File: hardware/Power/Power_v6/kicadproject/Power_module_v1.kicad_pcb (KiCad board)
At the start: 2 copper layers, 70 x 39.2 mm, 63 parts, among them J1 Conn_01x02, J3 USB_B_Micro, J4 Conn_01x02_battery, J5 Conn_01x06_programmer, J6 Conn_01x06_programmer, J7 610106249121, U1 BQ24040, U2 BQ25570, U3 VEML7700-TT, U4 PIC16F18446

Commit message: Power module: HW update new pinheaders + new case
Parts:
- added REF**: MountingHole_3mm, MountingHole:MountingHole_3mm, F.Cu at (154.0, 78.0)
- J3: moved to F.Cu
- moved J3 10.9 mm to (105.7, 105.2), turned to 0 degrees
- moved C2 0.84 mm to (150.8, 78.0)
- moved C3 0.55 mm to (148.8, 78.0)
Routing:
- net VUSB: track 67.8 -> 72.8 mm, vias 4 -> 5
- net GND: track 207.3 -> 203.7 mm, vias 82 -> 89
- net 3V3: track 72.9 -> 75.0 mm
- net VEML7700_SDA: track 62.6 -> 64.4 mm
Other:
- board size 70 x 39.2 mm -> 67.2 x 39.2 mm

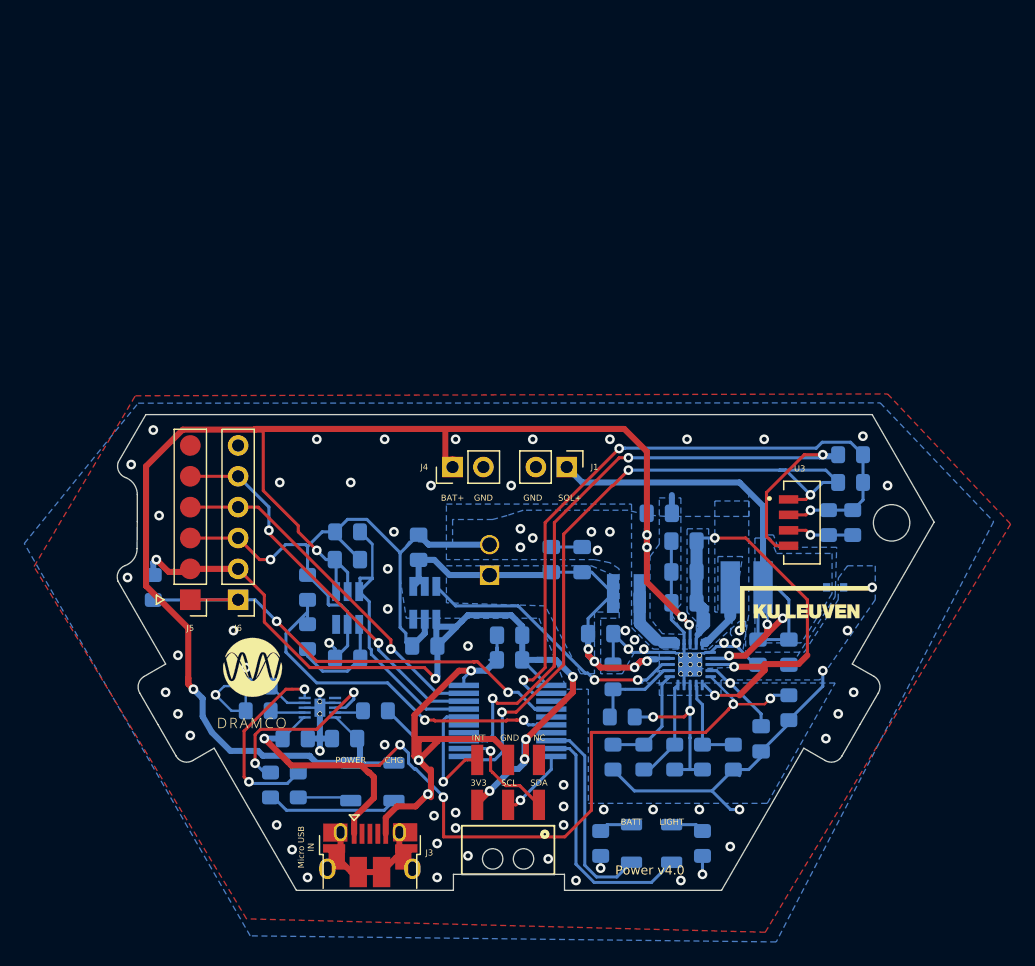
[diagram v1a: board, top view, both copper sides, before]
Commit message: Buttons + power HW update to support new casing
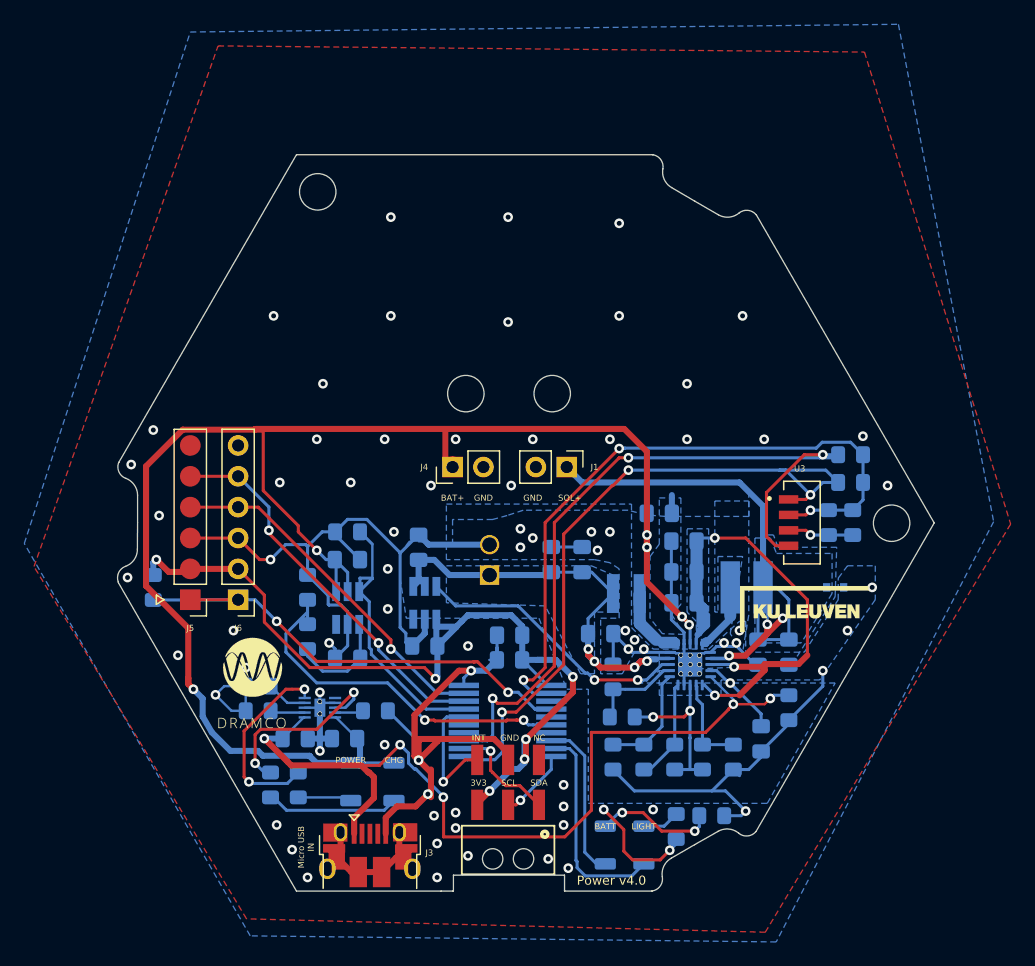
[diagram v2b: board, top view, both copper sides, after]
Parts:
- removed the REF** at (154.0, 78.0)
- added REF**: MountingHole_3mm, MountingHole:MountingHole_3mm, B.Cu at (126.1, 67.4)
- added REF**: MountingHole_3mm, MountingHole:MountingHole_3mm, B.Cu at (118.9, 67.4)
- added REF**: MountingHole_3mm, MountingHole:MountingHole_3mm, B.Cu at (154.0, 78.0)
- added REF**: MountingHole_3mm, MountingHole:MountingHole_3mm, B.Cu at (106.8, 50.7)
- moved R15 9.43 mm to (139.2, 102.1), turned to 0 degrees
- moved R14 2.57 mm to (136.3, 103.0)
- moved D3 2.29 mm to (133.6, 104.5)
- moved D4 2.16 mm to (130.4, 104.5)
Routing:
- net GND: track 203.7 -> 213.4 mm, vias 89 -> 88
- net Net-(D4-Pad1): track 2.76 -> 9.88 mm, vias 0 -> 2
- net LED1: track 17.0 -> 13.3 mm
- net LED0: track 20.4 -> 17.8 mm
- net (no net): vias 0 -> 1
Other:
- board size 67.2 x 39.2 mm -> 67.2 x 60.6 mm
